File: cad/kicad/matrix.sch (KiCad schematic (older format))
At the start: 32 parts

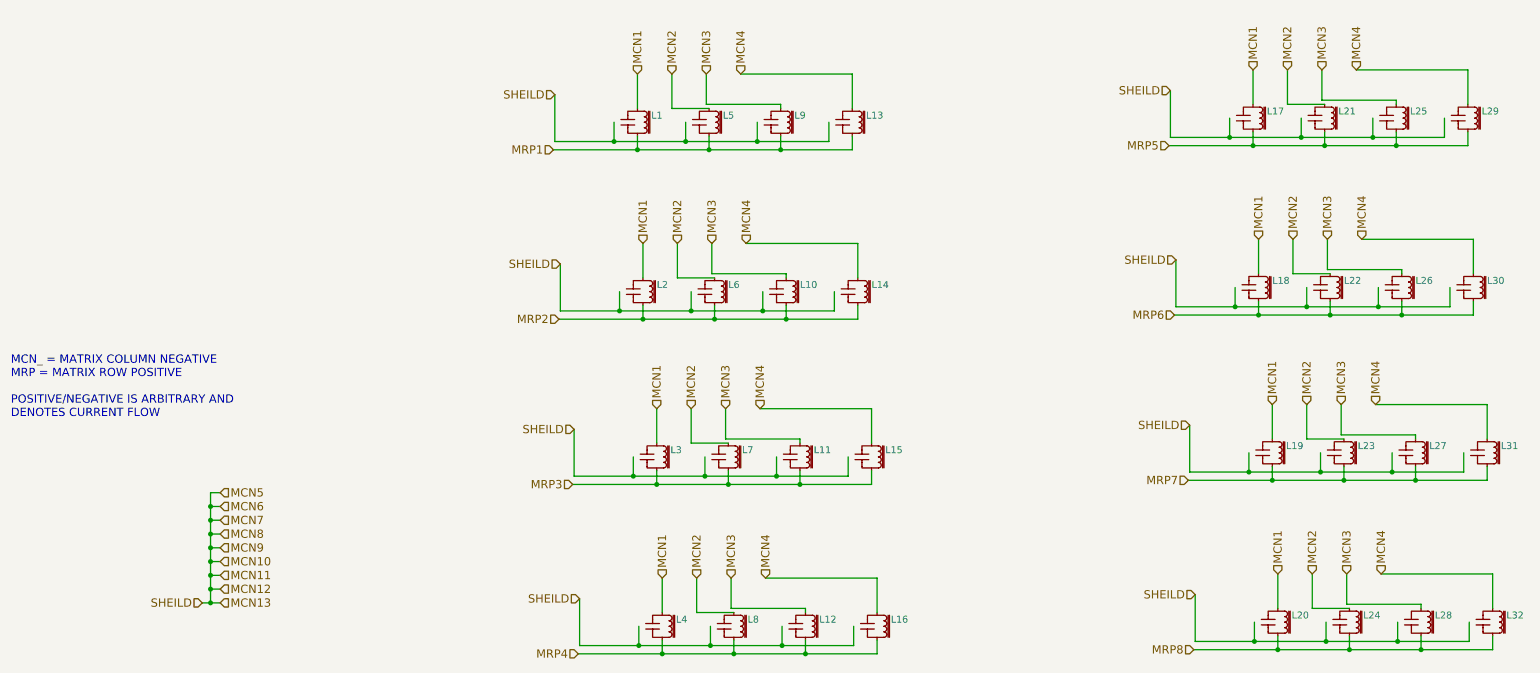
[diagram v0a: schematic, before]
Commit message: added logo, and started work on panelizing the demo pcb
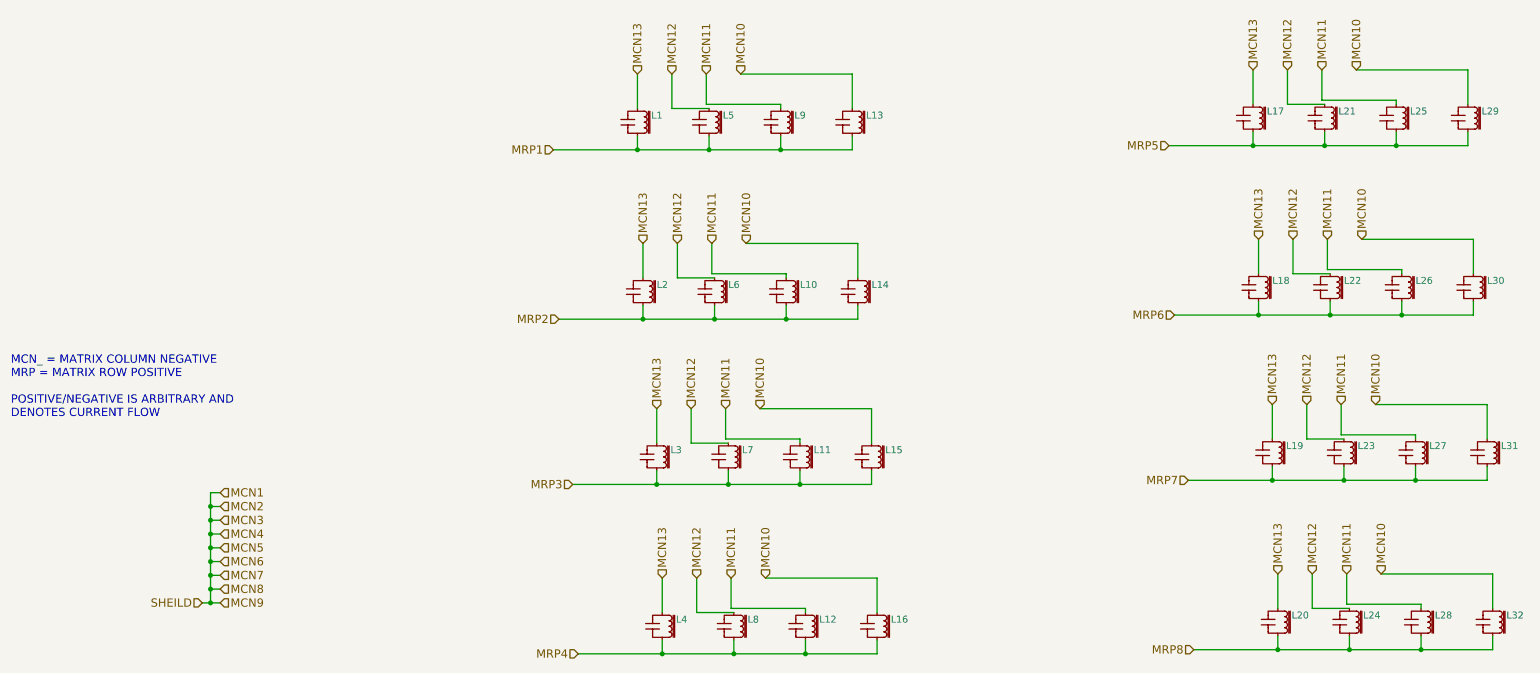
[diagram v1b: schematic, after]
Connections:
- wire segments 162 -> 114
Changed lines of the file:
@@
 Text Notes 1110 3870 0    60   ~ 0
 MCN_ = MATRIX COLUMN NEGATIVE\nMRP = MATRIX ROW POSITIVE\n\nPOSITIVE/NEGATIVE IS ARBITRARY AND \nDENOTES CURRENT FLOW
-Text HLabel 5660 1370 1    60   Input ~ 0
-MCN1
-Text HLabel 5910 1370 1    60   Input ~ 0
-MCN2
-Text HLabel 6160 1370 1    60   Input ~ 0
-MCN3
-Text HLabel 6410 1370 1    60   Input ~ 0
-MCN4
 Text HLabel 5050 1920 0    60   Input ~ 0
 MRP1
-Text HLabel 5060 1520 0    60   Input ~ 0
-SHEILD
 Text HLabel 5090 3150 0    60   Input ~ 0
 MRP2
@@
 Text HLabel 9660 4320 0    60   Input ~ 0
 MRP7
-Text HLabel 9700 5550 0    60   Input ~ 0
-MRP8
 Text HLabel 2500 5210 0    60   Input ~ 0
 SHEILD
@@
 	1    0    0    -1
 $EndComp
-Text HLabel 2630 4410 2    60   Input ~ 0
+Text HLabel 2630 4810 2    60   Input ~ 0
 MCN5
-Text HLabel 2630 4510 2    60   Input ~ 0
+Text HLabel 2630 4910 2    60   Input ~ 0
 MCN6
-Text HLabel 2630 4710 2    60   Input ~ 0
+Text HLabel 2630 5110 2    60   Input ~ 0
 MCN8
-Text HLabel 2630 4810 2    60   Input ~ 0
+Text HLabel 2630 5210 2    60   Input ~ 0
 MCN9
-Text HLabel 2630 4910 2    60   Input ~ 0
+Text HLabel 6410 1370 1    60   Input ~ 0
 MCN10
+Text HLabel 6160 1370 1    60   Input ~ 0
+MCN11
+Text HLabel 5910 1370 1    60   Input ~ 0
+MCN12
+Text HLabel 5660 1370 1    60   Input ~ 0
+MCN13
 Text HLabel 2630 5010 2    60   Input ~ 0
-MCN11
-Text HLabel 2630 5110 2    60   Input ~ 0
-MCN12
-Text HLabel 2630 5210 2    60   Input ~ 0
-MCN13
-Text HLabel 2630 4610 2    60   Input ~ 0
 MCN7
 Wire Wire Line
-	5060 1860 7050 1860
-Wire Wire Line
-	6010 1860 6010 1720
-Wire Wire Line
-	6530 1860 6530 1720
-Wire Wire Line
-	7050 1860 7050 1720
-Wire Wire Line
 	5660 1370 5660 1620
 Wire Wire Line
@@
 Wire Wire Line
 	7220 1370 7220 1620
-Connection ~ 6010 1860
-Connection ~ 6530 1860
-Wire Wire Line
-	5490 1860 5490 1720
-Wire Wire Line
-	5060 1860 5060 1520
-Connection ~ 5490 1860
 Wire Wire Line
 	5050 1920 7220 1920
@@
 Connection ~ 2560 5110
 Connection ~ 2560 5210
-Text HLabel 5700 2600 1    60   Input ~ 0
-MCN1
-Text HLabel 5950 2600 1    60   Input ~ 0
-MCN2
-Text HLabel 6200 2600 1    60   Input ~ 0
-MCN3
-Text HLabel 6450 2600 1    60   Input ~ 0
-MCN4
-Text HLabel 5100 2750 0    60   Input ~ 0
-SHEILD
 $Comp
 L L_Cap_Core_Iron L2
@@
 $EndComp
 Wire Wire Line
-	5100 3090 7090 3090
-Wire Wire Line
-	6050 3090 6050 2950
-Wire Wire Line
-	6570 3090 6570 2950
-Wire Wire Line
-	7090 3090 7090 2950
-Wire Wire Line
 	5700 2600 5700 2850
 Wire Wire Line
@@
 Wire Wire Line
 	7260 2600 7260 2850
-Connection ~ 6050 3090
-Connection ~ 6570 3090
-Wire Wire Line
-	5530 3090 5530 2950
-Wire Wire Line
-	5100 3090 5100 2750
-Connection ~ 5530 3090
 Wire Wire Line
 	5090 3150 7260 3150
@@
 	7260 3150 7260 3050
 Connection ~ 6740 3150
-Text HLabel 5800 3800 1    60   Input ~ 0
-MCN1
-Text HLabel 6050 3800 1    60   Input ~ 0
-MCN2
-Text HLabel 6300 3800 1    60   Input ~ 0
-MCN3
-Text HLabel 6550 3800 1    60   Input ~ 0
-MCN4
-Text HLabel 5200 3950 0    60   Input ~ 0
-SHEILD
 $Comp
 L L_Cap_Core_Iron L3
@@
 $EndComp
 Wire Wire Line
-	5200 4290 7190 4290
-Wire Wire Line
-	6150 4290 6150 4150
-Wire Wire Line
-	6670 4290 6670 4150
-Wire Wire Line
-	7190 4290 7190 4150
-Wire Wire Line
 	5800 3800 5800 4050
 Wire Wire Line
@@
 Wire Wire Line
 	7360 3800 7360 4050
-Connection ~ 6150 4290
-Connection ~ 6670 4290
-Wire Wire Line
-	5630 4290 5630 4150
-Wire Wire Line
-	5200 4290 5200 3950
-Connection ~ 5630 4290
 Wire Wire Line
 	5190 4350 7360 4350
@@
 	7360 4350 7360 4250
 Connection ~ 6840 4350
-Text HLabel 5840 5030 1    60   Input ~ 0
-MCN1
-Text HLabel 6090 5030 1    60   Input ~ 0
-MCN2
-Text HLabel 6340 5030 1    60   Input ~ 0
-MCN3
-Text HLabel 6590 5030 1    60   Input ~ 0
-MCN4
-Text HLabel 5240 5180 0    60   Input ~ 0
-SHEILD
 $Comp
 L L_Cap_Core_Iron L4
@@
 $EndComp
 Wire Wire Line
-	5240 5520 7230 5520
-Wire Wire Line
-	6190 5520 6190 5380
-Wire Wire Line
-	6710 5520 6710 5380
-Wire Wire Line
-	7230 5520 7230 5380
-Wire Wire Line
 	5840 5030 5840 5280
 Wire Wire Line
@@
 Wire Wire Line
 	7400 5030 7400 5280
-Connection ~ 6190 5520
-Connection ~ 6710 5520
-Wire Wire Line
-	5670 5520 5670 5380
-Wire Wire Line
-	5240 5520 5240 5180
-Connection ~ 5670 5520
 Wire Wire Line
 	5230 5580 7400 5580
@@
 	7400 5580 7400 5480
 Connection ~ 6880 5580
-Text HLabel 10130 1340 1    60   Input ~ 0
-MCN1
-Text HLabel 10380 1340 1    60   Input ~ 0
-MCN2
-Text HLabel 10630 1340 1    60   Input ~ 0
-MCN3
-Text HLabel 10880 1340 1    60   Input ~ 0
-MCN4
-Text HLabel 9530 1490 0    60   Input ~ 0
-SHEILD
 $Comp
 L L_Cap_Core_Iron L17
@@
 $EndComp
 Wire Wire Line
-	9530 1830 11520 1830
-Wire Wire Line
-	10480 1830 10480 1690
-Wire Wire Line
-	11000 1830 11000 1690
-Wire Wire Line
-	11520 1830 11520 1690
-Wire Wire Line
 	10130 1340 10130 1590
 Wire Wire Line
@@
 Wire Wire Line
 	11690 1340 11690 1590
-Connection ~ 10480 1830
-Connection ~ 11000 1830
-Wire Wire Line
-	9960 1830 9960 1690
-Wire Wire Line
-	9530 1830 9530 1490
-Connection ~ 9960 1830
 Wire Wire Line
 	9520 1890 11690 1890
@@
 	11690 1890 11690 1790
 Connection ~ 11170 1890
-Text HLabel 10170 2570 1    60   Input ~ 0
-MCN1
-Text HLabel 10420 2570 1    60   Input ~ 0
-MCN2
-Text HLabel 10670 2570 1    60   Input ~ 0
-MCN3
-Text HLabel 10920 2570 1    60   Input ~ 0
-MCN4
-Text HLabel 9570 2720 0    60   Input ~ 0
-SHEILD
 $Comp
 L L_Cap_Core_Iron L18
@@
 $EndComp
 Wire Wire Line
-	9570 3060 11560 3060
-Wire Wire Line
-	10520 3060 10520 2920
-Wire Wire Line
-	11040 3060 11040 2920
-Wire Wire Line
-	11560 3060 11560 2920
-Wire Wire Line
 	10170 2570 10170 2820
 Wire Wire Line
@@
 Wire Wire Line
 	11730 2570 11730 2820
-Connection ~ 10520 3060
-Connection ~ 11040 3060
-Wire Wire Line
-	10000 3060 10000 2920
-Wire Wire Line
-	9570 3060 9570 2720
-Connection ~ 10000 3060
 Wire Wire Line
 	9560 3120 11730 3120
@@
 	11730 3120 11730 3020
 Connection ~ 11210 3120
-Text HLabel 10270 3770 1    60   Input ~ 0
-MCN1
-Text HLabel 10520 3770 1    60   Input ~ 0
-MCN2
-Text HLabel 10770 3770 1    60   Input ~ 0
-MCN3
-Text HLabel 11020 3770 1    60   Input ~ 0
-MCN4
-Text HLabel 9670 3920 0    60   Input ~ 0
-SHEILD
 $Comp
 L L_Cap_Core_Iron L19
@@
 $EndComp
 Wire Wire Line
-	9670 4260 11660 4260
-Wire Wire Line
-	10620 4260 10620 4120
-Wire Wire Line
-	11140 4260 11140 4120
-Wire Wire Line
-	11660 4260 11660 4120
-Wire Wire Line
 	10270 3770 10270 4020
 Wire Wire Line
@@
 Wire Wire Line
 	11830 3770 11830 4020
-Connection ~ 10620 4260
-Connection ~ 11140 4260
-Wire Wire Line
-	10100 4260 10100 4120
-Wire Wire Line
-	9670 4260 9670 3920
-Connection ~ 10100 4260
 Wire Wire Line
 	9660 4320 11830 4320
@@
 	11830 4320 11830 4220
 Connection ~ 11310 4320
-Text HLabel 10310 5000 1    60   Input ~ 0
-MCN1
-Text HLabel 10560 5000 1    60   Input ~ 0
-MCN2
-Text HLabel 10810 5000 1    60   Input ~ 0
-MCN3
-Text HLabel 11060 5000 1    60   Input ~ 0
-MCN4
-Text HLabel 9710 5150 0    60   Input ~ 0
-SHEILD
 $Comp
 L L_Cap_Core_Iron L20
@@
 $EndComp
 Wire Wire Line
-	9710 5490 11700 5490
-Wire Wire Line
-	10660 5490 10660 5350
-Wire Wire Line
-	11180 5490 11180 5350
-Wire Wire Line
-	11700 5490 11700 5350
-Wire Wire Line
 	10310 5000 10310 5250
 Wire Wire Line
@@
 Wire Wire Line
 	11870 5000 11870 5250
-Connection ~ 10660 5490
-Connection ~ 11180 5490
-Wire Wire Line
-	10140 5490 10140 5350
-Wire Wire Line
-	9710 5490 9710 5150
-Connection ~ 10140 5490
 Wire Wire Line
 	9700 5550 11870 5550
@@
 	11870 5550 11870 5450
 Connection ~ 11350 5550
+Text HLabel 9700 5550 0    60   Input ~ 0
+MRP8
+Text HLabel 2630 4410 2    60   Input ~ 0
+MCN1
+Text HLabel 2630 4510 2    60   Input ~ 0
+MCN2
+Text HLabel 2630 4610 2    60   Input ~ 0
+MCN3
+Text HLabel 2630 4710 2    60   Input ~ 0
+MCN4
+Text HLabel 6450 2600 1    60   Input ~ 0
+MCN10
+Text HLabel 6200 2600 1    60   Input ~ 0
+MCN11
+Text HLabel 5950 2600 1    60   Input ~ 0
+MCN12
+Text HLabel 5700 2600 1    60   Input ~ 0
+MCN13
+Text HLabel 6550 3800 1    60   Input ~ 0
+MCN10
+Text HLabel 6300 3800 1    60   Input ~ 0
+MCN11
+Text HLabel 6050 3800 1    60   Input ~ 0
+MCN12
+Text HLabel 5800 3800 1    60   Input ~ 0
+MCN13
+Text HLabel 6590 5030 1    60   Input ~ 0
+MCN10
+Text HLabel 6340 5030 1    60   Input ~ 0
+MCN11
+Text HLabel 6090 5030 1    60   Input ~ 0
+MCN12
+Text HLabel 5840 5030 1    60   Input ~ 0
+MCN13
+Text HLabel 10880 1340 1    60   Input ~ 0
+MCN10
+Text HLabel 10630 1340 1    60   Input ~ 0
+MCN11
+Text HLabel 10380 1340 1    60   Input ~ 0
+MCN12
+Text HLabel 10130 1340 1    60   Input ~ 0
+MCN13
+Text HLabel 10920 2570 1    60   Input ~ 0
+MCN10
+Text HLabel 10670 2570 1    60   Input ~ 0
+MCN11
+Text HLabel 10420 2570 1    60   Input ~ 0
+MCN12
+Text HLabel 10170 2570 1    60   Input ~ 0
+MCN13
+Text HLabel 11020 3770 1    60   Input ~ 0
+MCN10
+Text HLabel 10770 3770 1    60   Input ~ 0
+MCN11
+Text HLabel 10520 3770 1    60   Input ~ 0
+MCN12
+Text HLabel 10270 3770 1    60   Input ~ 0
+MCN13
+Text HLabel 11060 5000 1    60   Input ~ 0
+MCN10
+Text HLabel 10810 5000 1    60   Input ~ 0
+MCN11
+Text HLabel 10560 5000 1    60   Input ~ 0
+MCN12
+Text HLabel 10310 5000 1    60   Input ~ 0
+MCN13
 $EndSCHEMATC
